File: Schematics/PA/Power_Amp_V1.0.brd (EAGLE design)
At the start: 83.5 x 76.5 mm, 105 parts, among them J1 4_PIN_AMPCONN, J10 OSTVN03A150, J11 SCREW_TERMINAL_4, J12 1725724, J13 1725724, J14 1725724, J5 OSTVN03A150, J6 OSTVN03A150, J7 OSTVN03A150, J8 OSTVN03A150, J9 OSTVN03A150, U1 LME49830, U2 LME49830, U3 LME49830

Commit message: updated PA
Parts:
- removed J10, J5, J6, J7, J8, J9: OSTVN03A150, Amplifier_Parts:OSTVN03A150
- PR1, PR2, PR3, PR4, PR5, PR6: device Power Resistors:2-1623788-1 -> rcl:0617V
- moved J12 145.9 mm to (41.0, 61.3), turned to 90 degrees
- moved C14 1.59 mm to (33.7, 71.8)
- moved C13 0.95 mm to (33.3, 67.4)
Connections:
- removed net N$1: C21.2, J6.P$1, R3.1, VR4.C
- removed net N$11: J5.P$3, PR2.P$4
- removed net N$110: PR5.P$3
- removed net N$2: C21.1, J6.P$2, R4.2, VR4.A, VR4.B
- removed net N$22: J7.P$1, PR1.P$3
- removed net N$23: C36.2, J9.P$1, R14.1, VR6.C
- removed net N$24: C36.1, J9.P$2, R15.2, VR6.A, VR6.B
- removed net N$26: C35.1, C37.1, J9.P$3, R15.1, U3.P11
- removed net N$29: J12.P$4
- removed net N$30: J8.P$2, R16.2, R18.1
- removed net N$32: J10.P$2, R16.1, R17.1
- removed net N$33: J8.P$3, PR4.P$4
- removed net N$34: J12.P$5
- removed net N$44: J12.P$6
- removed net N$45: J10.P$1, PR3.P$3
- removed net N$5: C20.1, C22.1, J6.P$3, R4.1, U2.P11
- removed net N$73: R46.1, R47.1
- removed net N$8: J5.P$2, R5.2, R7.1
- removed net N$9: J7.P$2, R5.1, R6.1
- new net B_NMOS_G: J13.P$2, R5.2, R7.1
- new net B_NMOS_S: J13.P$3, PR2.2
- new net B_PMOS_G: J13.P$8, R5.1, R6.1
- new net B_PMOS_S: J13.P$7, PR1.1
- new net B_VBE_B: C21.1, J13.P$5, R4.2, VR4.A, VR4.B
- new net B_VBE_C: C21.2, J13.P$6, R3.1, VR4.C
- new net B_VBE_E: C20.1, C22.1, J13.P$4, R4.1, U2.P11
- new net L_NMOS_G: J14.P$2, R16.2, R18.1
- new net L_NMOS_S: J14.P$3, PR4.2
- new net L_PMOS_G: J14.P$8, R16.1, R17.1
- new net L_PMOS_S: J14.P$7, PR3.1
- new net L_VBE_B: C36.1, J14.P$5, R15.2, VR6.A, VR6.B
- new net L_VBE_C: C36.2, J14.P$6, R14.1, VR6.C
- new net L_VBE_E: C35.1, C37.1, J14.P$4, R15.1, U3.P11
- new net R_PMOS_S: J12.P$7, PR5.1
- net N$12: now also PR1.2, PR2.1; no longer PR1.P$4, PR2.P$3
- net N$75: now also PR5.2, PR6.1; no longer PR5.P$4, PR6.P$3
- net N$77: now also PR3.2, PR4.1; no longer PR3.P$4, PR4.P$3
- net R_NMOS_S: now also PR6.2; no longer PR6.P$4
- net R_PMOS_G: now also R46.1, R47.1; no longer J12.P$7
- net R_VBE_B: now also J12.P$5
- net R_VBE_C: now also J12.P$6
- net R_VBE_E: now also J12.P$4
- net V+: now also J13.P$1, J14.P$1; no longer J5.P$1, J8.P$1
- net V-: now also J13.P$9, J14.P$9; no longer J10.P$3, J7.P$3
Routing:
- net R_PMOS_S: track 0.00 -> 16.3 mm
- net R_PMOS_G: track 0.00 -> 12.7 mm
- net N$73: track 11.6 -> 0.00 mm
- net R_VBE_B: track 15.2 -> 23.7 mm
- net N$110: track 4.16 -> 0.00 mm
- net V-: track 107.5 -> 111.3 mm
- net R_NMOS_S: track 14.5 -> 16.4 mm
- net V+: track 79.9 -> 80.6 mm
- net R_NMOS_G: track 13.8 -> 13.1 mm

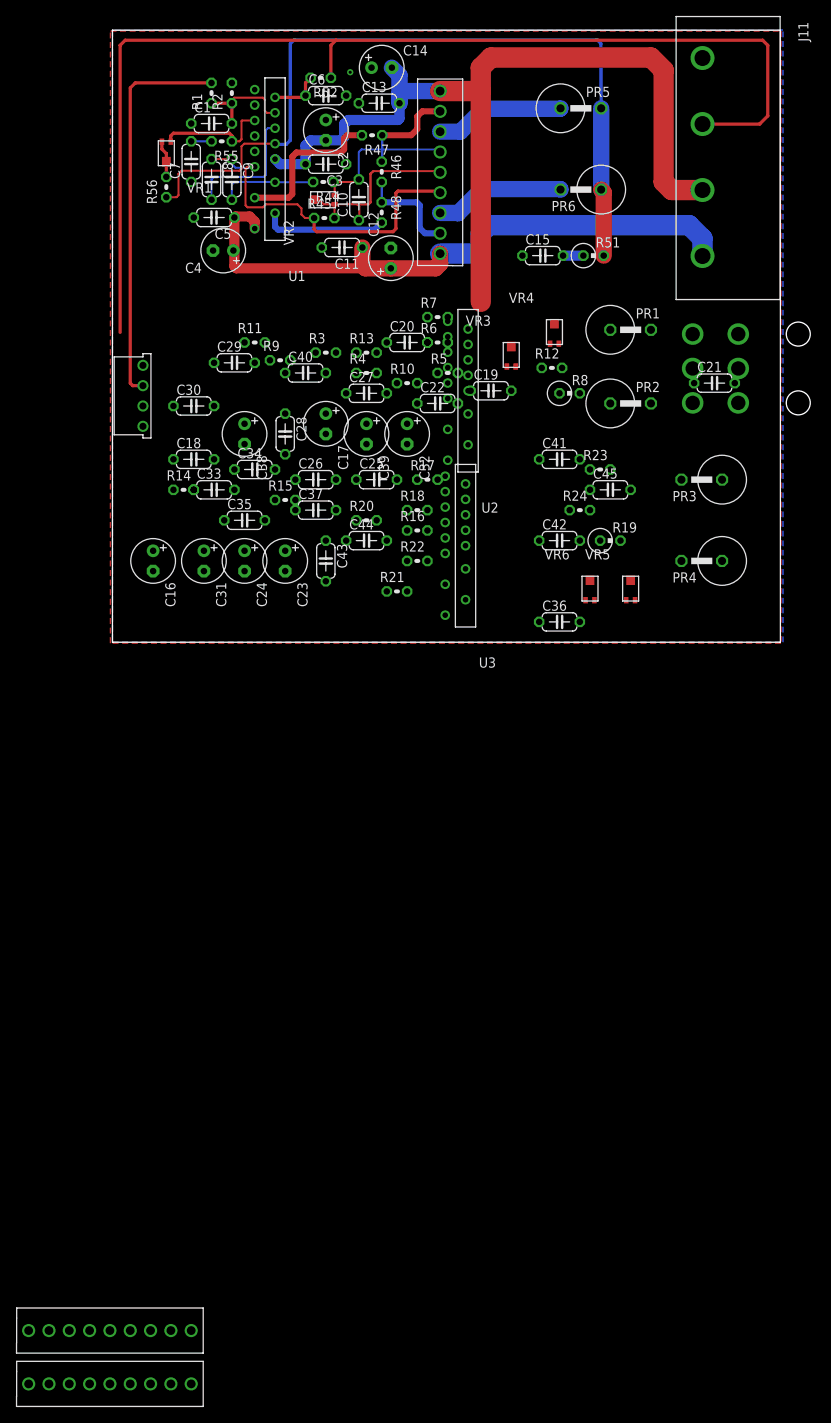
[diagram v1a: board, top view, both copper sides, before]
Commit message: reduced total size of PA board
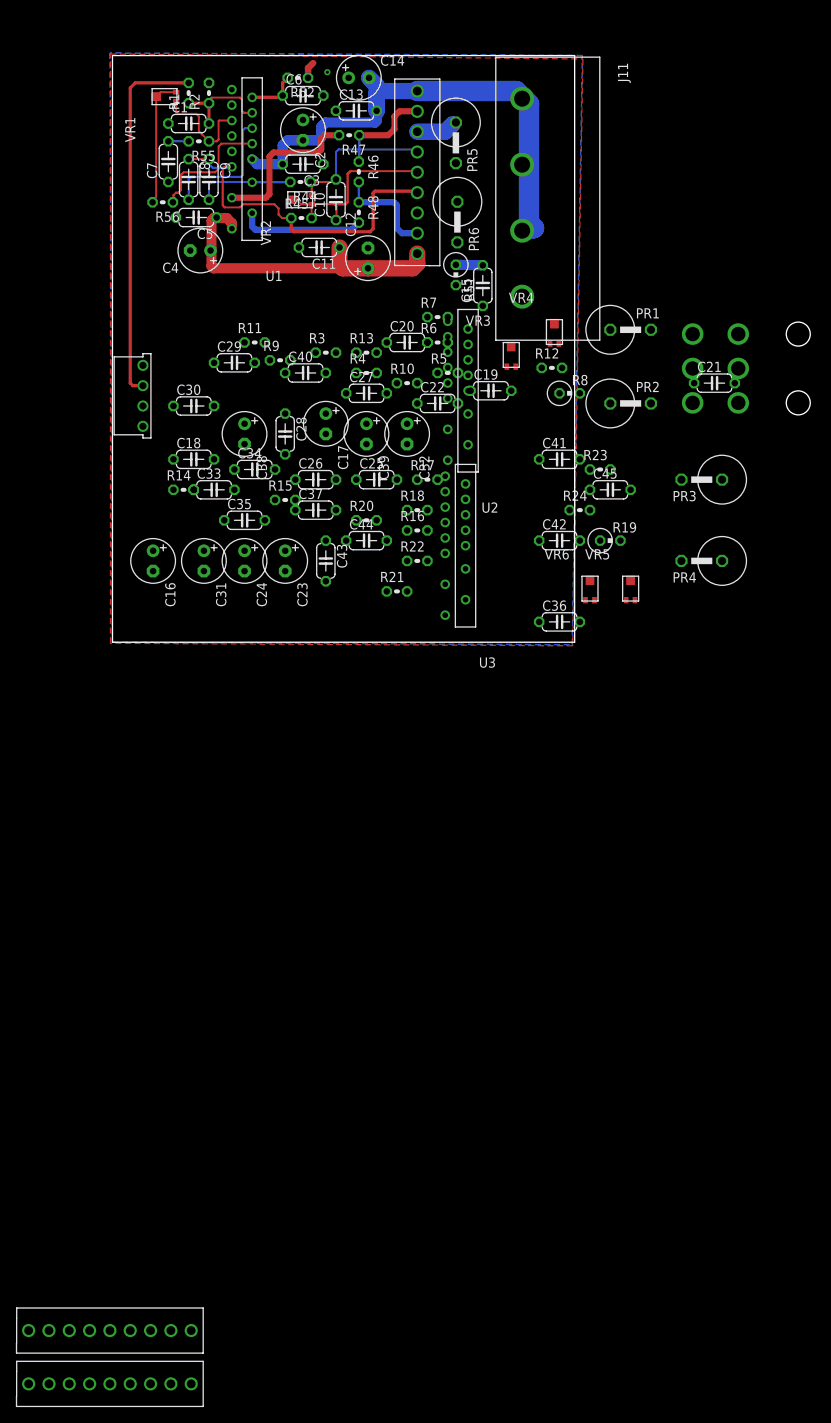
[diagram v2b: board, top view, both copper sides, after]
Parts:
- moved J11 23.1 mm to (50.5, 54.7)
- moved R51 17.4 mm to (42.9, 45.9), turned to 270 degrees
- moved PR5 16.2 mm to (42.9, 62.4), turned to 270 degrees
- moved PR6 16.0 mm to (43.1, 52.5), turned to 270 degrees
- moved C15 8.38 mm to (46.3, 44.6), turned to 90 degrees
- moved VR1 6.73 mm to (6.86, 68.2), turned to 90 degrees
- moved C14 3.13 mm to (30.8, 70.5)
- moved C13 3.01 mm to (30.5, 66.4)
- moved C11 2.86 mm to (25.8, 49.3)
- moved C12 2.86 mm to (31.9, 48.0)
- moved C2 2.86 mm to (23.8, 64.0)
- moved C3 2.86 mm to (23.8, 59.8)
- moved C6 2.86 mm to (23.8, 68.3)
- moved J12 2.86 mm to (38.1, 61.3)
- moved R45 2.86 mm to (23.6, 53.0)
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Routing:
- net MUTE: track 139.7 -> 2.10 mm
- net N$75: track 99.6 -> 16.2 mm
- net V-: track 111.3 -> 65.3 mm
- net V+: track 80.6 -> 42.0 mm
- net R_NMOS_S: track 16.4 -> 0.00 mm
- net N$40: track 4.63 -> 16.1 mm
- net R_PMOS_S: track 16.3 -> 4.84 mm
- net RIGHT: track 49.0 -> 46.2 mm
- net N$31: track 14.7 -> 13.3 mm
- net N$84: track 2.54 -> 3.37 mm
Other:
- board size 83.5 x 76.5 mm -> 57.8 x 73.3 mm

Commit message: made changes to my PA board
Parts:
- moved J14 135.3 mm to (38.1, 37.8), turned to 90 degrees
- moved J13 106.6 mm to (38.1, 14.3), turned to 90 degrees
- moved PR3 50.1 mm to (25.7, 34.9)
- moved C21 47.3 mm to (28.6, 40.0)
- moved C45 42.2 mm to (22.9, 3.81)
- moved U$17 38.4 mm to (42.2, 30.8)
- moved R19 35.1 mm to (27.9, 5.40)
- moved VR5 33.4 mm to (31.4, 8.57)
- moved VR6 29.0 mm to (30.8, 4.45)
- moved R24 28.7 mm to (30.8, 8.89)
- moved PR4 28.6 mm to (45.1, 11.1)
- moved U2 27.9 mm to (20.0, 38.4)
- moved PR1 27.9 mm to (45.7, 18.7)
- moved U3 27.2 mm to (20.0, 17.5)
- moved C41 24.5 mm to (32.1, 17.1)
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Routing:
- net RIGHT: track 46.2 -> 0.00 mm
- net V-: track 65.3 -> 33.4 mm
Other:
- board size 57.8 x 73.3 mm -> 46.7 x 73.3 mm

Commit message: Finished My PA and made changes to Carlos' PA
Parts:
- removed J11: SCREW_TERMINAL_4, Amplifier_Parts:SCREW_TERMINAL_4
- added J2: 1984633, Amplifier_Parts:1984633
- added J3, J4, J5: 2TERMINAL_SPEAKER, Amplifier_Parts:2TERMINAL_SPEAKER
- U$17: value MOLEX_6P -> (none); device Amplifier_Parts:MOLEX_6P -> PersonalLogos:MUSHROOM
- moved VR3 47.7 mm to (3.49, 47.0), turned to 90 degrees
- moved U$17 45.2 mm to (34.9, 75.4), turned to 180 degrees
- moved R23 40.1 mm to (7.62, 17.5), turned to 180 degrees
- moved C19 40.0 mm to (7.30, 32.4), turned to 180 degrees
- moved R12 39.8 mm to (7.30, 41.6), turned to 180 degrees
- moved C24 37.7 mm to (28.9, 45.7), turned to 90 degrees
- moved C16 35.4 mm to (20.6, 41.9)
- moved R22 34.0 mm to (6.67, 23.2), turned to 90 degrees
- moved C22 32.9 mm to (8.57, 37.1), turned to 90 degrees
- moved R10 32.1 mm to (8.57, 47.6), turned to 90 degrees
- moved VR5 32.1 mm to (3.17, 23.8), turned to 90 degrees
- moved R21 31.5 mm to (8.89, 23.2), turned to 90 degrees
- moved C20 30.8 mm to (6.03, 37.1), turned to 90 degrees
- moved C40 30.1 mm to (26.0, 3.64), turned to 270 degrees
- moved R13 29.0 mm to (2.86, 34.3), turned to 180 degrees
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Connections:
- net BASS renamed N$1
- net GND: now also J2.P$1, J3.P$2, J4.P$2, J5.P$2; no longer J11.1, U$17.P$2, U$17.P$4, U$17.P$6
- net MUTE: now also J2.P$2; no longer J11.2
- net N$12: now also J4.P$1; no longer U$17.P$3
- net N$75: now also J3.P$1; no longer U$17.P$1
- net N$77: now also J5.P$1; no longer U$17.P$5
- net V+: now also J2.P$4; no longer J11.4
- net V-: now also J2.P$3; no longer J11.3
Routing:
- net V+: track 42.0 -> 243.7 mm
- net V-: track 33.4 -> 195.3 mm
- net MUTE: track 2.10 -> 146.0 mm
- net RIGHT: track 0.00 -> 76.3 mm
- net N$12: track 0.00 -> 71.4 mm
- net N$75: track 16.2 -> 81.5 mm
- net N$77: track 0.00 -> 64.5 mm
- net N$1: track 0.00 -> 55.3 mm
- net L_VBE_E: track 0.00 -> 46.0 mm
- net B_VBE_E: track 0.00 -> 45.8 mm
- net LEFT: track 0.00 -> 28.4 mm
- net B_VBE_B: track 0.00 -> 25.4 mm
- net L_VBE_B: track 0.00 -> 23.2 mm
- net L_VBE_C: track 0.00 -> 20.7 mm
- net B_VBE_C: track 0.00 -> 19.6 mm
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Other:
- board size 46.7 x 73.3 mm -> 50.5 x 76.8 mm
- board text added: "3 Channel Power Amplifier"
- board text added: "CT Nov, 2015 CM"
